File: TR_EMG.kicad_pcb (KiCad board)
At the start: 4 copper layers, 118.1 x 101.6 mm, 118 parts, among them J1 1727230, J2 1727230, J3 1844236, J4 MJ-3523-SMT-TR, J5 MJ-3523-SMT-TR, J6 MJ-3523-SMT-TR, J7 MJ-3523-SMT-TR, U1 ADS1115IDGSR, U101 INA115BU, U111 LT1169CS8-PBF, U112 LT1169CS8-PBF, U201 INA115BU, U211 LT1169CS8-PBF, U212 LT1169CS8-PBF, U301 INA115BU, U311 LT1169CS8-PBF, U312 LT1169CS8-PBF, U401 INA115BU, U411 LT1169CS8-PBF, U412 LT1169CS8-PBF

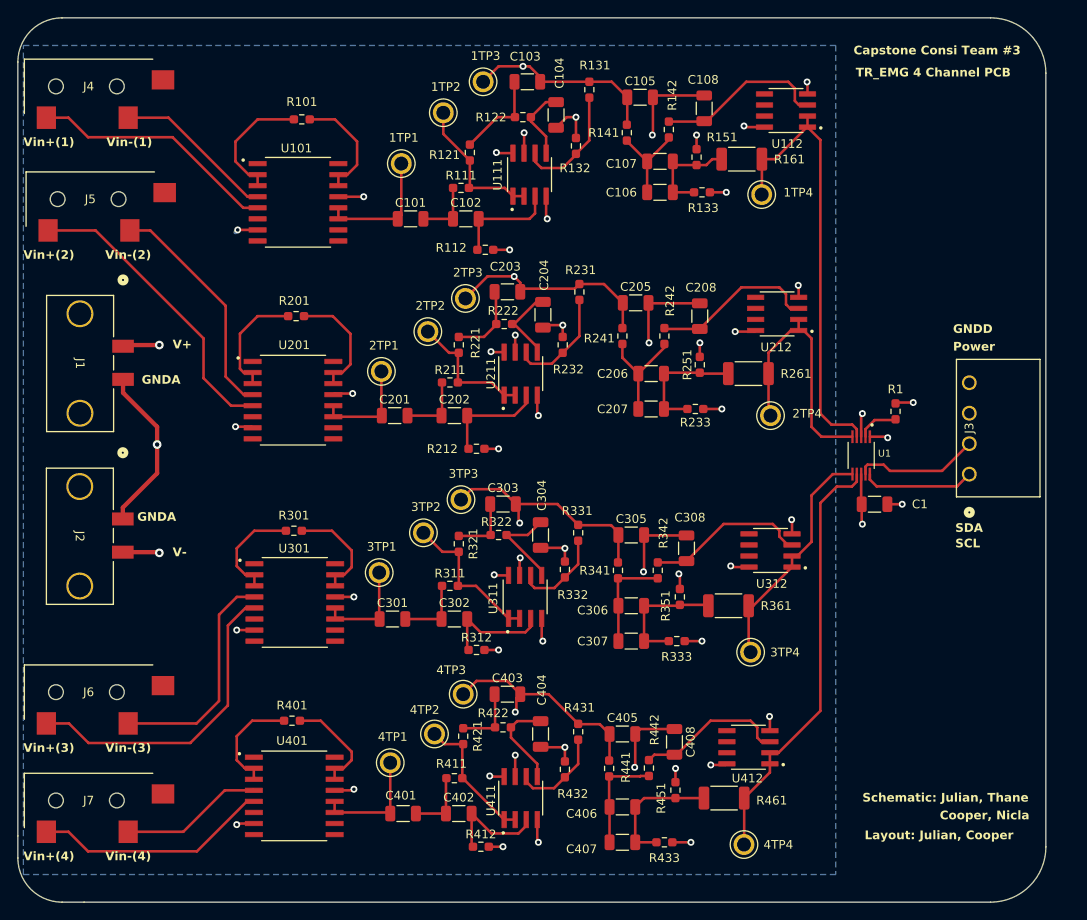
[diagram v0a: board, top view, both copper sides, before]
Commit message: added mounting holes, board ready for export
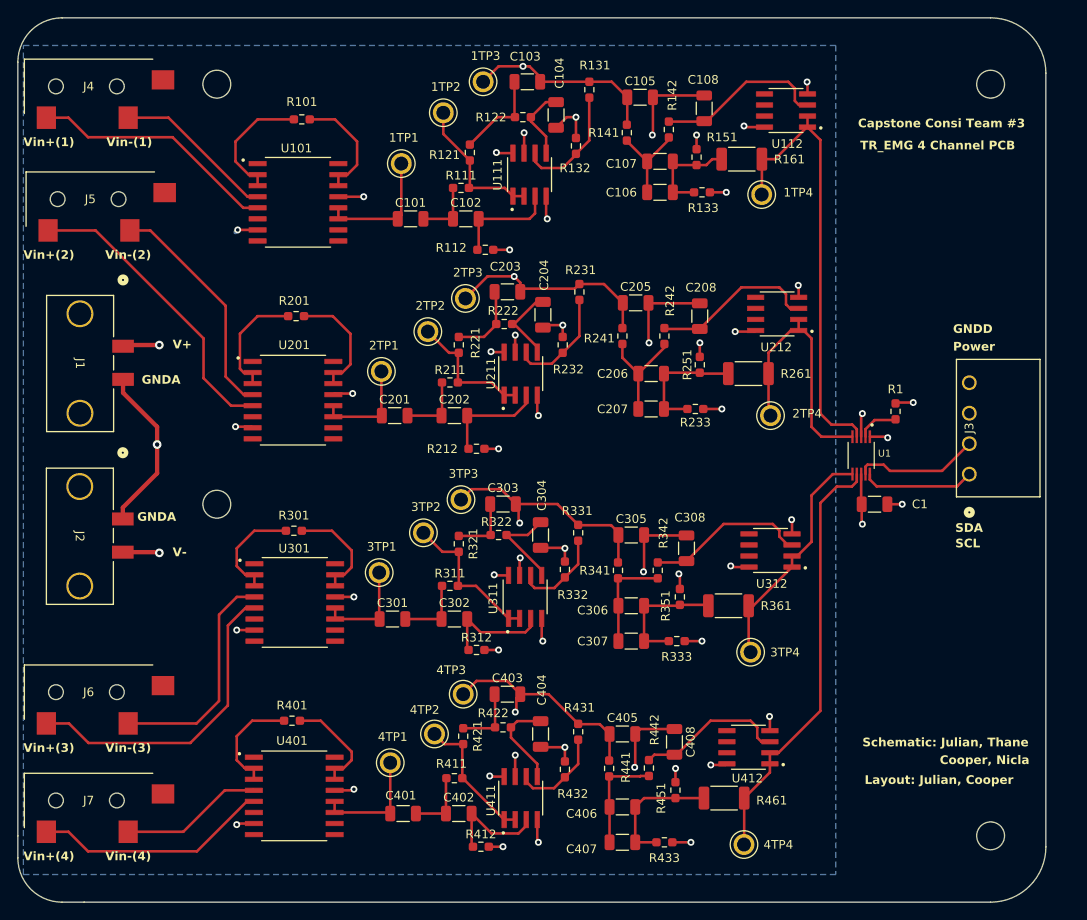
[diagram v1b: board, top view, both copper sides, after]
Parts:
- added REF**: MountingHole_3.2mm_M3, MountingHole:MountingHole_3.2mm_M3, F.Cu at (200.7, 132.1)
- added REF**: MountingHole_3.2mm_M3, MountingHole:MountingHole_3.2mm_M3, F.Cu at (111.8, 94.0)
- added REF**: MountingHole_3.2mm_M3, MountingHole:MountingHole_3.2mm_M3, F.Cu at (200.7, 45.7)
- added REF**: MountingHole_3.2mm_M3, MountingHole:MountingHole_3.2mm_M3, F.Cu at (111.8, 45.7)
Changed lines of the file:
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@@
     )
   )
+  (footprint "MountingHole:MountingHole_3.2mm_M3" (layer "F.Cu")
+    (at 200.66 132.08)
+    (descr "Mounting Hole 3.2mm, no annular, M3")
+    (tags "mounting hole 3.2mm no annular m3")
+    (attr exclude_from_pos_files exclude_from_bom)
+    (fp_text reference "REF**" (at 0 -4.2) (layer "F.SilkS") hide
+        (effects (font (size 1 1) (thickness 0.15)))
+    )
+    (fp_text value "MountingHole_3.2mm_M3" (at 0 4.2) (layer "F.Fab")
+        (effects (font (size 1 1) (thickness 0.15)))
+    )
+    (fp_text user "${REFERENCE}" (at 0 0) (layer "F.Fab")
+        (effects (font (size 1 1) (thickness 0.15)))
+    )
+    (fp_circle (center 0 0) (end 3.2 0)
+      (stroke (width 0.15) (type solid)) (fill none) (layer "Cmts.User"))
+    (fp_circle (center 0 0) (end 3.45 0)
+      (stroke (width 0.05) (type solid)) (fill none) (layer "F.CrtYd"))
+    (pad "" np_thru_hole circle (at 0 0) (size 3.2 3.2) (drill 3.2) (layers "*.Cu" "*.Mask"))
+  )
   (footprint "footprints:INA-SOIC127P1030X265-16N" (layer "F.Cu")
     (at 120.5103 82.022298)
@@
         (effects (font (size 1 1) (thickness 0.15)))
     )
-    (fp_text value "LT1169CS8-PBF" (at -44.6598 -53.1886 90) (layer "F.Fab")
+    (fp_text value "LT1169CS8-PBF" (at 2.520298 3.1877 90) (layer "F.Fab")
         (effects (font (size 0.64 0.64) (thickness 0.15)))
     )
@@
       (solder_mask_margin 0.102))
   )
+  (footprint "MountingHole:MountingHole_3.2mm_M3" (layer "F.Cu")
+    (at 111.76 93.98)
+    (descr "Mounting Hole 3.2mm, no annular, M3")
+    (tags "mounting hole 3.2mm no annular m3")
+    (attr exclude_from_pos_files exclude_from_bom)
+    (fp_text reference "REF**" (at 0 -4.2) (layer "F.SilkS") hide
+        (effects (font (size 1 1) (thickness 0.15)))
+    )
+    (fp_text value "MountingHole_3.2mm_M3" (at 0 4.2) (layer "F.Fab")
+        (effects (font (size 1 1) (thickness 0.15)))
+    )
+    (fp_text user "${REFERENCE}" (at 0 0) (layer "F.Fab")
+        (effects (font (size 1 1) (thickness 0.15)))
+    )
+    (fp_circle (center 0 0) (end 3.2 0)
+      (stroke (width 0.15) (type solid)) (fill none) (layer "Cmts.User"))
+    (fp_circle (center 0 0) (end 3.45 0)
+      (stroke (width 0.05) (type solid)) (fill none) (layer "F.CrtYd"))
+    (pad "" np_thru_hole circle (at 0 0) (size 3.2 3.2) (drill 3.2) (layers "*.Cu" "*.Mask"))
+  )
   (footprint "footprints:TP_5012" (layer "F.Cu")
     (at 175.3743 83.800298)
@@
     )
   )
+  (footprint "MountingHole:MountingHole_3.2mm_M3" (layer "F.Cu")
+    (at 200.66 45.72)
+    (descr "Mounting Hole 3.2mm, no annular, M3")
+    (tags "mounting hole 3.2mm no annular m3")
+    (attr exclude_from_pos_files exclude_from_bom)
+    (fp_text reference "REF**" (at 0 -4.2) (layer "F.SilkS") hide
+        (effects (font (size 1 1) (thickness 0.15)))
+    )
+    (fp_text value "MountingHole_3.2mm_M3" (at 0 4.2) (layer "F.Fab")
+        (effects (font (size 1 1) (thickness 0.15)))
+    )
+    (fp_text user "${REFERENCE}" (at 0 0) (layer "F.Fab")
+        (effects (font (size 1 1) (thickness 0.15)))
+    )
+    (fp_circle (center 0 0) (end 3.2 0)
+      (stroke (width 0.15) (type solid)) (fill none) (layer "Cmts.User"))
+    (fp_circle (center 0 0) (end 3.45 0)
+      (stroke (width 0.05) (type solid)) (fill none) (layer "F.CrtYd"))
+    (pad "" np_thru_hole circle (at 0 0) (size 3.2 3.2) (drill 3.2) (layers "*.Cu" "*.Mask"))
+  )
   (footprint "Resistor_SMD:R_0603_1608Metric_Pad0.98x0.95mm_HandSolder" (layer "F.Cu")
     (at 146.9273 49.510298)
@@
     )
   )
+  (footprint "MountingHole:MountingHole_3.2mm_M3" (layer "F.Cu")
+    (at 111.76 45.72)
+    (descr "Mounting Hole 3.2mm, no annular, M3")
+    (tags "mounting hole 3.2mm no annular m3")
+    (attr exclude_from_pos_files exclude_from_bom)
+    (fp_text reference "REF**" (at 0 -4.2) (layer "F.SilkS") hide
+        (effects (font (size 1 1) (thickness 0.15)))
+    )
+    (fp_text value "MountingHole_3.2mm_M3" (at 0 4.2) (layer "F.Fab")
+        (effects (font (size 1 1) (thickness 0.15)))
+    )
+    (fp_text user "${REFERENCE}" (at 0 0) (layer "F.Fab")
+        (effects (font (size 1 1) (thickness 0.15)))
+    )
+    (fp_circle (center 0 0) (end 3.2 0)
+      (stroke (width 0.15) (type solid)) (fill none) (layer "Cmts.User"))
+    (fp_circle (center 0 0) (end 3.45 0)
+      (stroke (width 0.05) (type solid)) (fill none) (layer "F.CrtYd"))
+    (pad "" np_thru_hole circle (at 0 0) (size 3.2 3.2) (drill 3.2) (layers "*.Cu" "*.Mask"))
+  )
   (footprint "Resistor_SMD:R_0603_1608Metric_Pad0.98x0.95mm_HandSolder" (layer "F.Cu")
     (at 166.878 54.102 90)
@@
         (effects (font (size 1 1) (thickness 0.15)))
     )
-    (fp_text value "13k" (at -49.775 -54.965 90) (layer "F.Fab")
+    (fp_text value "13k" (at -0.678202 -1.3843 90) (layer "F.Fab")
         (effects (font (size 1 1) (thickness 0.15)))
     )
@@
     (effects (font (size 1 1) (thickness 0.2) bold) (justify left bottom))
   )
-  (gr_text "Layout: Julian, Cooper" (at 186.182 132.588) (layer "F.SilkS")
+  (gr_text "Layout: Julian, Cooper" (at 186.182 126.238) (layer "F.SilkS")
     (effects (font (size 1 1) (thickness 0.2) bold) (justify left bottom))
   )
@@
     (effects (font (size 1 1) (thickness 0.2) bold) (justify left bottom))
   )
-  (gr_text "Schematic: Julian, Thane" (at 185.928 128.27) (layer "F.SilkS")
+  (gr_text "Schematic: Julian, Thane" (at 185.928 121.92) (layer "F.SilkS")
     (effects (font (size 1 1) (thickness 0.2) bold) (justify left bottom))
   )
@@
     (effects (font (size 1 1) (thickness 0.2) bold) (justify left bottom))
   )
-  (gr_text "Capstone Consi Team #3" (at 184.912 42.418) (layer "F.SilkS")
+  (gr_text "Capstone Consi Team #3" (at 185.42 50.8) (layer "F.SilkS")
     (effects (font (size 1 1) (thickness 0.2) bold) (justify left bottom))
   )
-  (gr_text "TR_EMG 4 Channel PCB" (at 185.166 44.958) (layer "F.SilkS")
+  (gr_text "TR_EMG 4 Channel PCB" (at 185.674 53.34) (layer "F.SilkS")
     (effects (font (size 1 1) (thickness 0.2) bold) (justify left bottom))
   )
@@
     (effects (font (size 1 1) (thickness 0.2) bold) (justify left bottom))
   )
-  (gr_text "Cooper, Nicla" (at 194.818 130.302) (layer "F.SilkS")
+  (gr_text "Cooper, Nicla" (at 194.818 123.952) (layer "F.SilkS")
     (effects (font (size 1 1) (thickness 0.2) bold) (justify left bottom))
   )
